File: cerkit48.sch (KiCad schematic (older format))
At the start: 99 parts, among them J1 QWIIC_CONNECTORJS-1MM, SW1 SW_Push_Dual_x2, SW10 CherryMX, SW11 CherryMX, SW12 CherryMX, SW13 CherryMX, SW14 CherryMX, SW15 CherryMX, SW16 CherryMX, SW17 CherryMX, SW18 CherryMX, SW19 CherryMX, SW2 CherryMX, SW20 CherryMX, SW21 CherryMX, SW22 CherryMX, SW23 CherryMX, SW24 CherryMX, SW25 CherryMX, SW26 CherryMX, SW27 CherryMX, SW28 CherryMX, SW29 CherryMX, SW3 CherryMX, SW30 CherryMX, SW31 CherryMX, SW32 CherryMX, SW33 CherryMX, SW34 CherryMX, SW35 CherryMX, SW36 CherryMX, SW37 CherryMX, SW38 CherryMX, SW39 CherryMX, SW4 CherryMX, SW40 CherryMX, SW41 CherryMX, SW42 CherryMX, SW43 CherryMX, SW44 CherryMX, SW45 CherryMX, SW46 CherryMX, SW47 CherryMX, SW48 CherryMX, SW49 CherryMX, SW5 CherryMX, SW6 CherryMX, SW7 CherryMX, SW8 CherryMX, SW9 CherryMX, U1 proton_c

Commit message: updated schematic
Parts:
- J1: footprint 1X04_1MM_RA -> Connectors:1X04_1MM_RA
- SW1: footprint (none) -> Button_Switch_THT:SW_PUSH_6mm
- SW10, SW11, SW12, SW13, SW14, SW15, SW16, SW17, SW18, SW19, SW2, SW20, SW21, SW22, SW23, SW24, SW25, SW26, SW27, SW28, SW29, SW3, SW30, SW31, SW32, SW33, SW34, SW35, SW36, SW37, SW38, SW39, SW4, SW40, SW41, SW42, SW43, SW44, SW45, SW46, SW47, SW48, SW49, SW5, SW6, SW7, SW8, SW9: footprint (none) -> MX_Only:MXOnly-1U
- U1: footprint (none) -> proton_c:proton_c
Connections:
- net GND1 is gone; now on net GND: SW1.1 (C), U1.GND
- net GND2 is gone; now on net GND: J1.1 (GND), U1.GND
- net COL0: no longer SW10.1, SW11.1, SW12.1, SW13.1, SW15.1, SW16.1, SW17.1, SW18.1, SW19.1, SW20.1, SW21.1, SW22.1, SW23.1, SW24.1, SW25.1, SW27.1, SW28.1, SW29.1, SW3.1, SW30.1, SW31.1, SW32.1, SW33.1, SW34.1, SW35.1, SW36.1, SW37.1, SW39.1, SW4.1, SW40.1, SW41.1, SW42.1, SW43.1, SW44.1, SW45.1, SW46.1, SW47.1, SW48.1, SW49.1, SW5.1, SW6.1, SW7.1, SW8.1, SW9.1
- net COL1: now also SW15.1, SW27.1, SW3.1, SW39.1
- net COL10: now also SW12.1, SW24.1, SW36.1, SW48.1
- net COL11: now also SW13.1, SW25.1, SW37.1, SW49.1
- net COL2: now also SW16.1, SW28.1, SW4.1, SW40.1
- net COL3: now also SW17.1, SW29.1, SW41.1, SW5.1
- net COL4: now also SW18.1, SW30.1, SW42.1, SW6.1
- net COL5: now also SW19.1, SW31.1, SW43.1, SW7.1
- net COL6: now also SW20.1, SW32.1, SW44.1, SW8.1
- net COL7: now also SW21.1, SW33.1, SW45.1, SW9.1
- net COL8: now also SW10.1, SW22.1, SW34.1, SW46.1
- net COL9: now also SW11.1, SW23.1, SW35.1, SW47.1
- net ROW1: no longer D25.1 (K), D26.1 (K), D27.1 (K), D28.1 (K), D29.1 (K), D30.1 (K), D31.1 (K), D32.1 (K), D33.1 (K), D37.1 (K), D38.1 (K), D39.1 (K), D40.1 (K), D41.1 (K), D42.1 (K), D43.1 (K), D44.1 (K), D45.1 (K), D46.1 (K), D47.1 (K), D48.1 (K)
- net ROW2: now also D25.1 (K), D26.1 (K), D27.1 (K), D28.1 (K), D29.1 (K), D30.1 (K), D31.1 (K), D32.1 (K), D33.1 (K)
- net ROW3: now also D37.1 (K), D38.1 (K), D39.1 (K), D40.1 (K), D41.1 (K), D42.1 (K), D43.1 (K), D44.1 (K), D45.1 (K), D46.1 (K), D47.1 (K), D48.1 (K)
- net GND: now reaches U1.GND
- net VCC renamed 3.3V
- no-connect marks 23 -> 22
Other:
- moved on the sheet: SW1A

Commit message: updated schematic to close some tracks
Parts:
- SW10, SW11, SW12, SW13, SW14, SW15, SW16, SW17, SW18, SW19, SW2, SW20, SW21, SW22, SW23, SW24, SW25, SW26, SW27, SW28, SW29, SW3, SW30, SW31, SW32, SW33, SW34, SW35, SW36, SW37, SW38, SW39, SW4, SW40, SW41, SW42, SW43, SW44, SW45, SW46, SW47, SW48, SW49, SW5, SW6, SW7, SW8, SW9: footprint MX_Only:MXOnly-1U -> MX_Only:MXOnly-1U-NoLED
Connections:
- net ROW0: now also D10.1 (K), D11.1 (K), D12.1 (K)
- net ROW1: now also D22.1 (K), D23.1 (K), D24.1 (K)
- net ROW2: now also D34.1 (K), D35.1 (K), D36.1 (K)

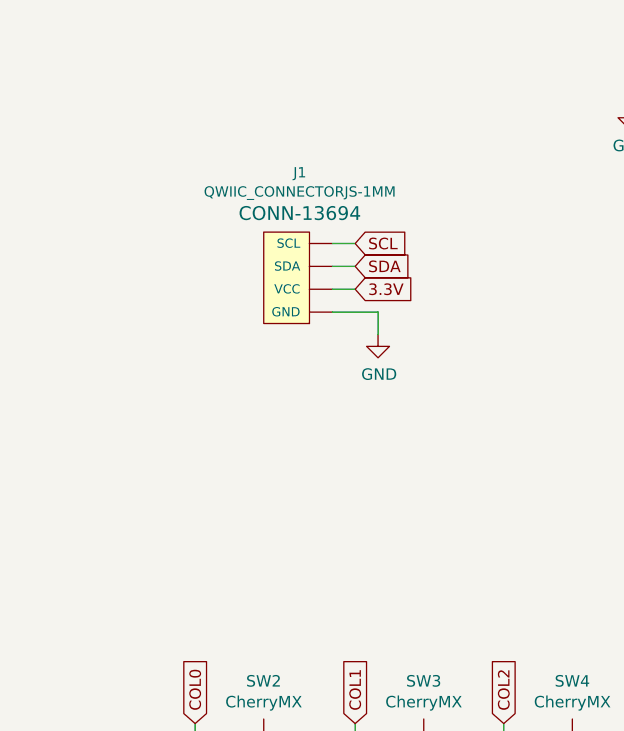
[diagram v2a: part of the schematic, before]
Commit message: finished PCB and ran DRC with no errors
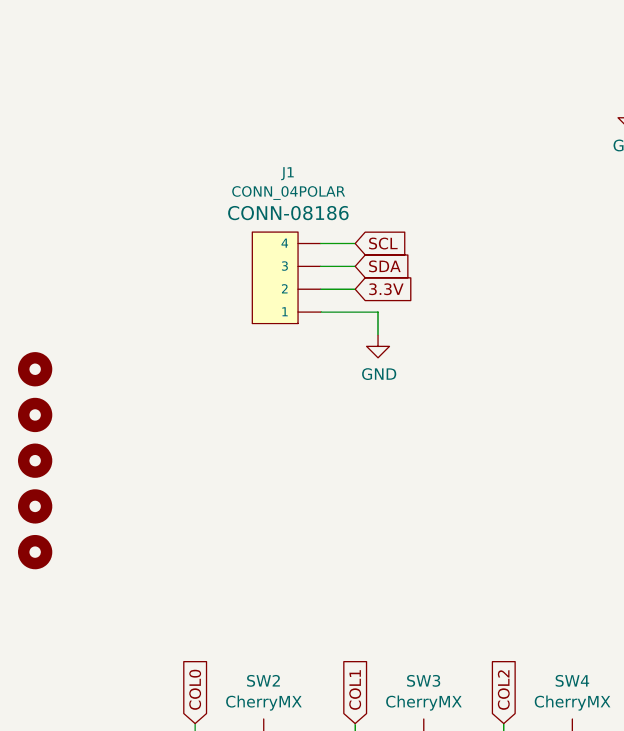
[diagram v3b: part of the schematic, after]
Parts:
- removed J1: QWIIC_CONNECTORJS-1MM, Connectors:1X04_1MM_RA, symbol SparkFun-Connectors:QWIIC_CONNECTORJS-1MM
- added H1, H2, H3, H4, H5: MountingHole, MountingHole:MountingHole_3.2mm_M3, symbol Mechanical:MountingHole
- added J1: CONN_04POLAR, Connectors:MOLEX-1X4, symbol SparkFun-Connectors:CONN_04POLAR
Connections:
- net 3.3V: now also J1.2
- net GND: now also J1.1
- net SCL: now also J1.4
- net SDA: now also J1.3
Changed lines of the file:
@@
 Wire Wire Line
 	6450 1350 6650 1350
-$Comp
-L SparkFun-Connectors:QWIIC_CONNECTORJS-1MM J1
-U 1 1 5EFE0071
-P 2400 2100
-F 0 "J1" H 2358 2710 45  0000 C CNN
-F 1 "QWIIC_CONNECTORJS-1MM" H 2358 2626 45  0000 C CNN
-F 2 "Connectors:1X04_1MM_RA" H 2400 2600 20  0001 C CNN
-F 3 "" H 2400 2100 50  0001 C CNN
-F 4 "CONN-13694" H 2358 2531 60  0000 C CNN "Field4"
-	1    2400 2100
-	1    0    0    -1
-$EndComp
 Text GLabel 2600 2000 2    50   Input ~ 0
 3.3V
@@
 Wire Wire Line
 	6450 1150 6650 1150
-Wire Wire Line
-	2600 2000 2500 2000
 Wire Wire Line
 	4150 1650 4400 1650
@@
 	6700 850  6450 850
 Wire Wire Line
-	2500 1800 2600 1800
-Wire Wire Line
-	2600 1900 2500 1900
-Wire Wire Line
 	2400 4750 2400 4700
 Wire Wire Line
@@
 $EndComp
 Wire Wire Line
-	2500 2100 2700 2100
-Wire Wire Line
 	2700 2100 2700 2200
 Wire Wire Line
@@
 	7650 4350 8300 4350
 Connection ~ 7650 4350
+$Comp
+L SparkFun-Connectors:CONN_04POLAR J1
+U 1 1 5EF1EDAE
+P 2350 2100
+F 0 "J1" H 2308 2710 45  0000 C CNN
+F 1 "CONN_04POLAR" H 2308 2626 45  0000 C CNN
+F 2 "Connectors:MOLEX-1X4" H 2350 2600 20  0001 C CNN
+F 3 "" H 2350 2100 50  0001 C CNN
+F 4 "CONN-08186" H 2308 2531 60  0000 C CNN "Field4"
+	1    2350 2100
+	1    0    0    -1
+$EndComp
+Wire Wire Line
+	2600 1800 2450 1800
+Wire Wire Line
+	2450 1900 2600 1900
+Wire Wire Line
+	2450 2000 2600 2000
+Wire Wire Line
+	2450 2100 2700 2100
+$Comp
+L Mechanical:MountingHole H1
+U 1 1 5EFA9DB5
+P 1200 2350
+F 0 "H1" H 1300 2396 50  0001 L CNN
+F 1 "MountingHole" H 1300 2350 50  0001 L CNN
+F 2 "MountingHole:MountingHole_3.2mm_M3" H 1200 2350 50  0001 C CNN
+F 3 "~" H 1200 2350 50  0001 C CNN
+	1    1200 2350
+	1    0    0    -1
+$EndComp
+$Comp
+L Mechanical:MountingHole H2
+U 1 1 5EFD9E24
+P 1200 2550
+F 0 "H2" H 1300 2596 50  0001 L CNN
+F 1 "MountingHole" H 1300 2550 50  0001 L CNN
+F 2 "MountingHole:MountingHole_3.2mm_M3" H 1200 2550 50  0001 C CNN
+F 3 "~" H 1200 2550 50  0001 C CNN
+	1    1200 2550
+	1    0    0    -1
+$EndComp
+$Comp
+L Mechanical:MountingHole H3
+U 1 1 5EFE920E
+P 1200 2750
+F 0 "H3" H 1300 2796 50  0001 L CNN
+F 1 "MountingHole" H 1300 2750 50  0001 L CNN
+F 2 "MountingHole:MountingHole_3.2mm_M3" H 1200 2750 50  0001 C CNN
+F 3 "~" H 1200 2750 50  0001 C CNN
+	1    1200 2750
+	1    0    0    -1
+$EndComp
+$Comp
+L Mechanical:MountingHole H4
+U 1 1 5EFF8634
+P 1200 2950
+F 0 "H4" H 1300 2996 50  0001 L CNN
+F 1 "MountingHole" H 1300 2950 50  0001 L CNN
+F 2 "MountingHole:MountingHole_3.2mm_M3" H 1200 2950 50  0001 C CNN
+F 3 "~" H 1200 2950 50  0001 C CNN
+	1    1200 2950
+	1    0    0    -1
+$EndComp
+$Comp
+L Mechanical:MountingHole H5
+U 1 1 5F007A46
+P 1200 3150
+F 0 "H5" H 1300 3196 50  0001 L CNN
+F 1 "MountingHole" H 1300 3150 50  0001 L CNN
+F 2 "MountingHole:MountingHole_3.2mm_M3" H 1200 3150 50  0001 C CNN
+F 3 "~" H 1200 3150 50  0001 C CNN
+	1    1200 3150
+	1    0    0    -1
+$EndComp
 $EndSCHEMATC

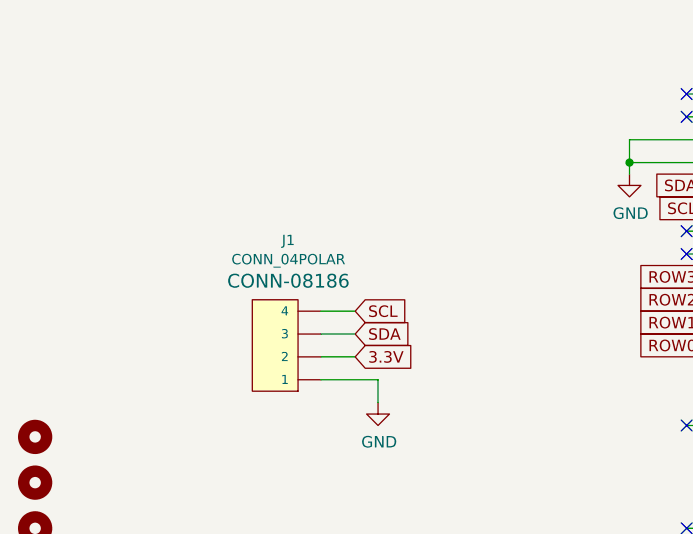
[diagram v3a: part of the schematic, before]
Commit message: Added new I2C Pin Header footprint
I needed the I2C legend printed on the silkscreen layer, so I made a new footprint.
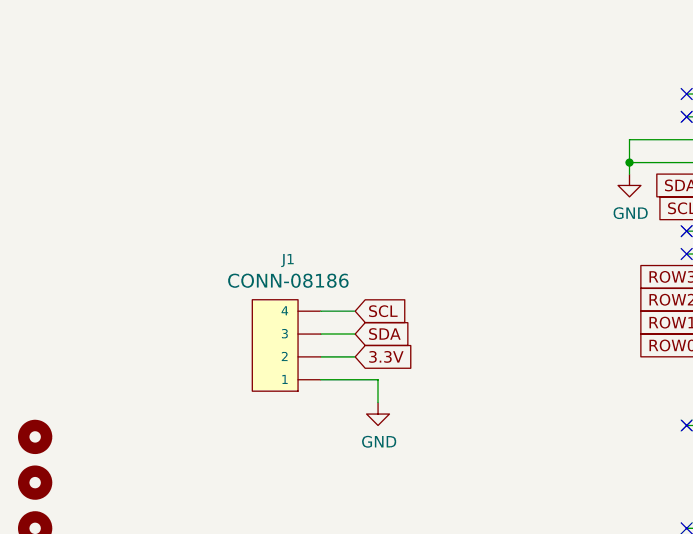
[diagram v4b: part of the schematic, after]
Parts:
- J1: value CONN_04POLAR -> I2C; footprint Connectors:MOLEX-1X4 -> footprints:PIN_HEADER_I2C
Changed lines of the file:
@@
 U 1 1 5EF1EDAE
 P 2350 2100
-F 0 "J1" H 2308 2710 45  0000 C CNN
-F 1 "CONN_04POLAR" H 2308 2626 45  0000 C CNN
-F 2 "Connectors:MOLEX-1X4" H 2350 2600 20  0001 C CNN
+F 0 "J1" H 2308 2626 45  0000 C CNN
+F 1 "I2C" H 2308 2626 45  0001 C CNN
+F 2 "footprints:PIN_HEADER_I2C" H 2350 2600 20  0001 C CNN
 F 3 "" H 2350 2100 50  0001 C CNN
 F 4 "CONN-08186" H 2308 2531 60  0000 C CNN "Field4"

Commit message: Updated schematic details and footprint references
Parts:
- J1: footprint footprints:PIN_HEADER_I2C -> cerkit48:PIN_HEADER_I2C
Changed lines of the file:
@@
 encoding utf-8
 Sheet 1 1
-Title ""
+Title "cerkit 48 4x12 Ortholinear Keyboard"
 Date ""
-Rev ""
-Comp ""
+Rev "1.0"
+Comp "cerkit.com"
 Comment1 ""
 Comment2 ""
@@
 F 0 "J1" H 2308 2626 45  0000 C CNN
 F 1 "I2C" H 2308 2626 45  0001 C CNN
-F 2 "footprints:PIN_HEADER_I2C" H 2350 2600 20  0001 C CNN
+F 2 "cerkit48:PIN_HEADER_I2C" H 2350 2600 20  0001 C CNN
 F 3 "" H 2350 2100 50  0001 C CNN
 F 4 "CONN-08186" H 2308 2531 60  0000 C CNN "Field4"

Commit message: Updated schematic to use project symbols from submodules
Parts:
- removed SW10, SW11, SW12, SW13, SW14, SW15, SW16, SW17, SW18, SW19, SW20, SW21, SW22, SW23, SW24, SW25, SW26, SW27, SW28, SW29, SW3, SW30, SW31, SW32, SW33, SW34, SW35, SW36, SW37, SW38, SW39, SW4, SW40, SW41, SW42, SW43, SW44, SW45, SW46, SW47, SW48, SW49, SW5, SW6, SW7, SW8, SW9: CherryMX, MX_Only:MXOnly-1U-NoLED, symbol CherryMX:CherryMX
- added SW10, SW11, SW12, SW13, SW15, SW16, SW17, SW18, SW19, SW2, SW20, SW21, SW22, SW23, SW24, SW25, SW26, SW27, SW28, SW29, SW3, SW30, SW31, SW32, SW33, SW34, SW35, SW36, SW37, SW38, SW39, SW4, SW40, SW41, SW42, SW43, SW44, SW45, SW46, SW47, SW48, SW49, SW5, SW6, SW7, SW8, SW9: CherryMX, MX_Only:MXOnly-1U-NoLED, symbol MX_Alps_Hybrid:MX-NoLED
- SW14: renamed from SW2; symbol CherryMX:CherryMX -> MX_Alps_Hybrid:MX-NoLED
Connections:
- wire segments 246 -> 198
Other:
- moved on the sheet: D1, D13, D25, D37, SW1A, U1
